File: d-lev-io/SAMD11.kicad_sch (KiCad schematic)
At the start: 32 parts, among them J6 PROG_HDR, SW1 SW_Push, SW2 SW_Push, SW3 SW_Push, U3 ATSAMD11D14A-M

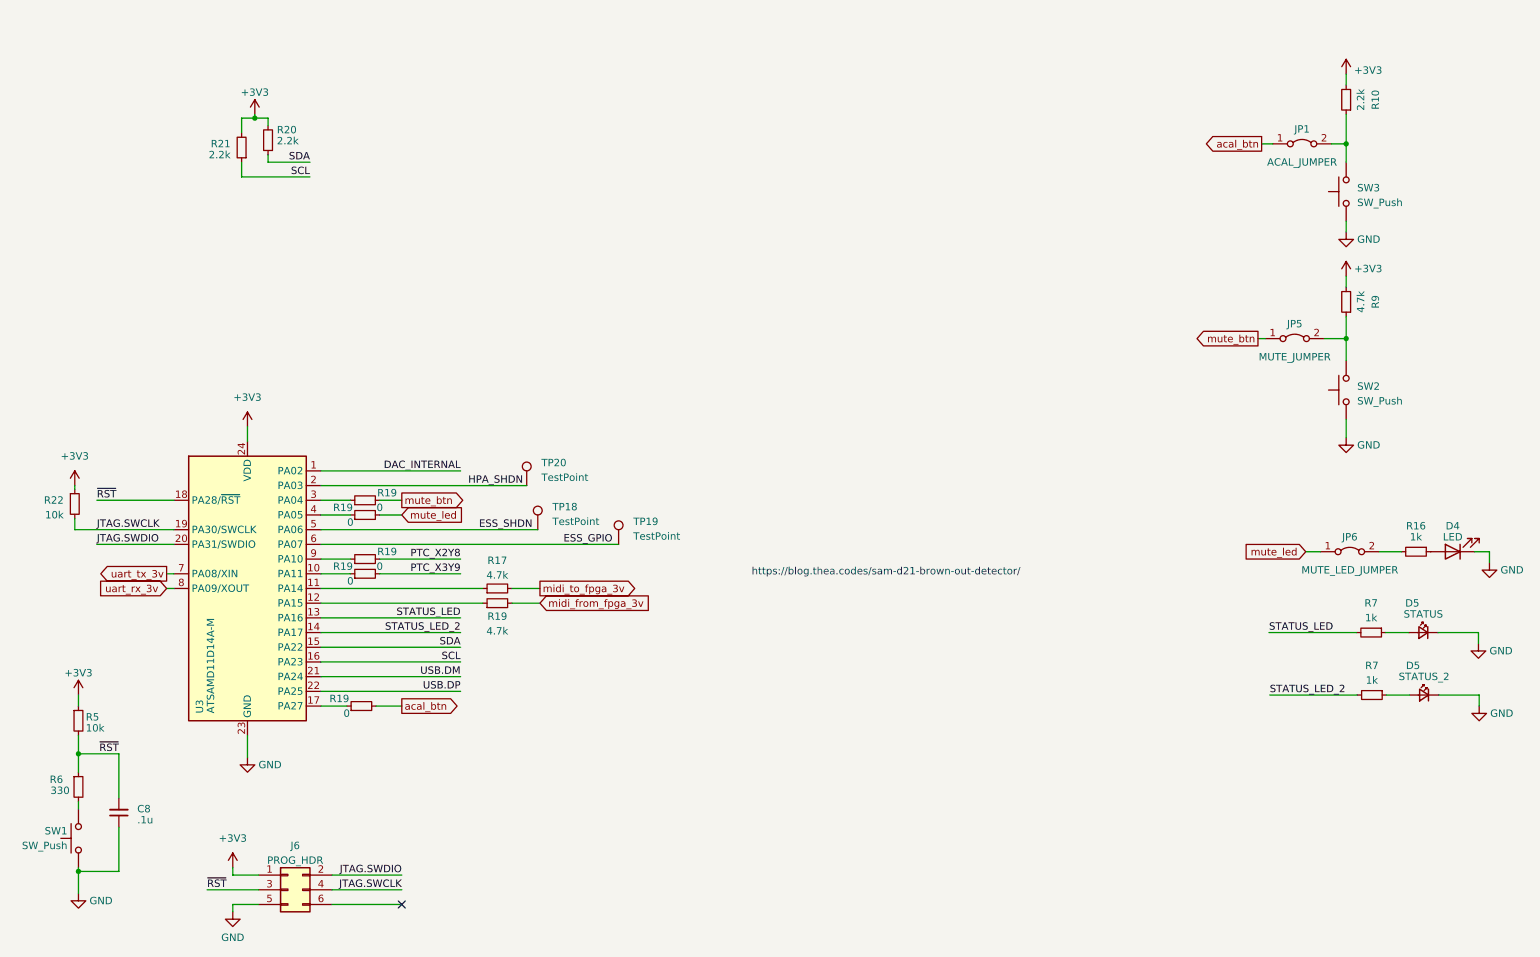
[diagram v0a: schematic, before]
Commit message: Added DAC schematic to I/O board
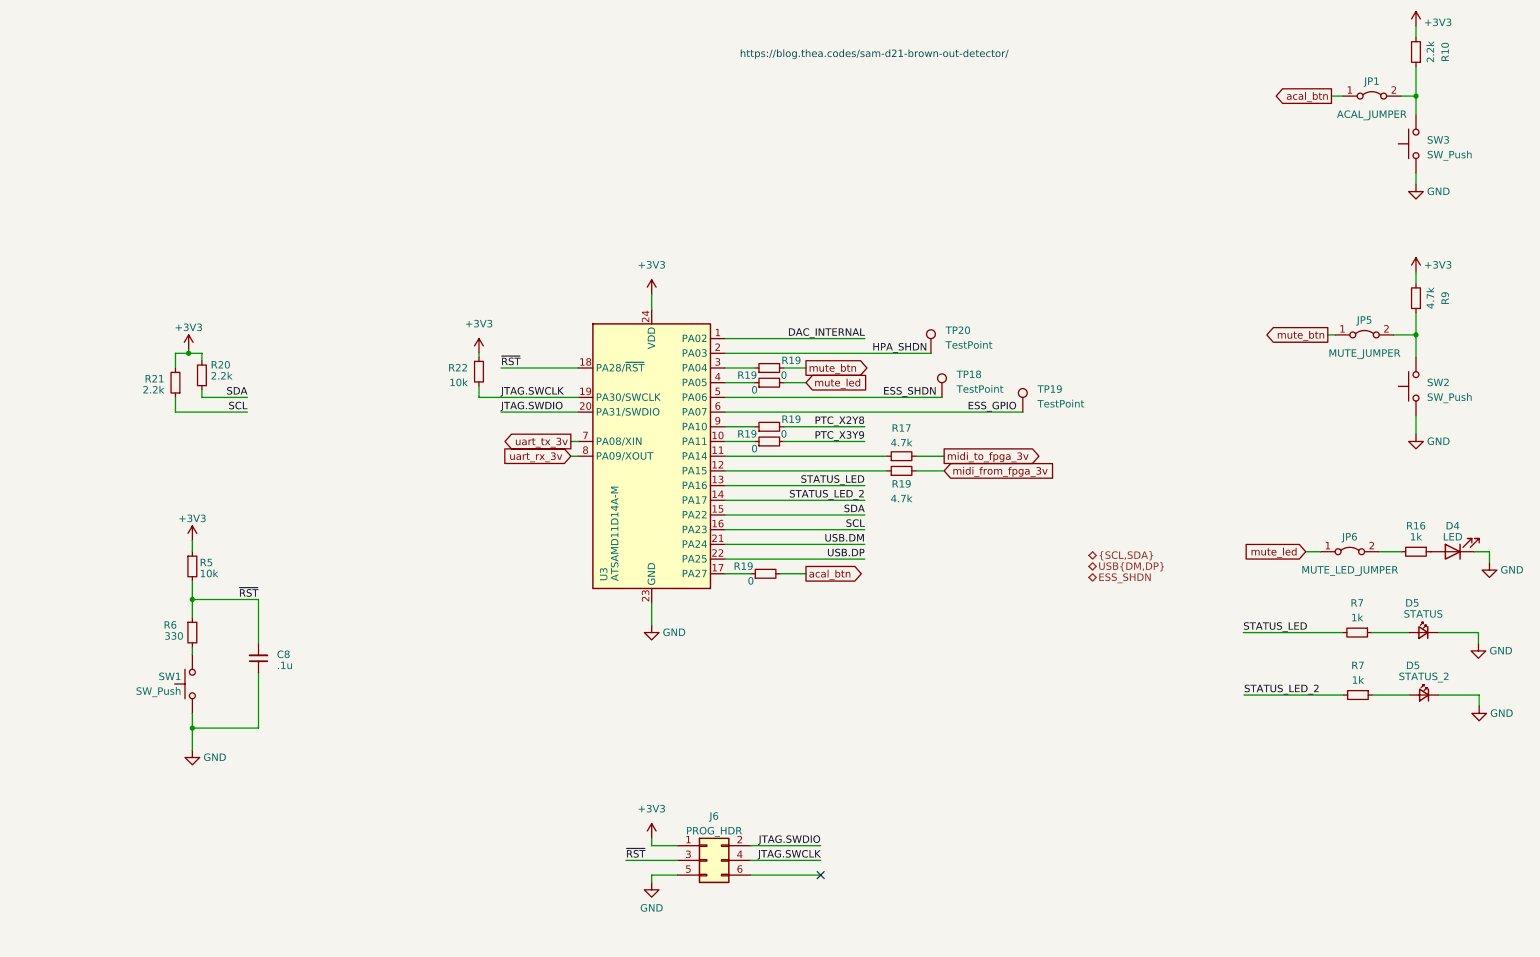
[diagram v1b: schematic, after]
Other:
- moved on the sheet: C8, J6, JP1, JP5, R10, R17, R19, R20, R21, R22, R5, R6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

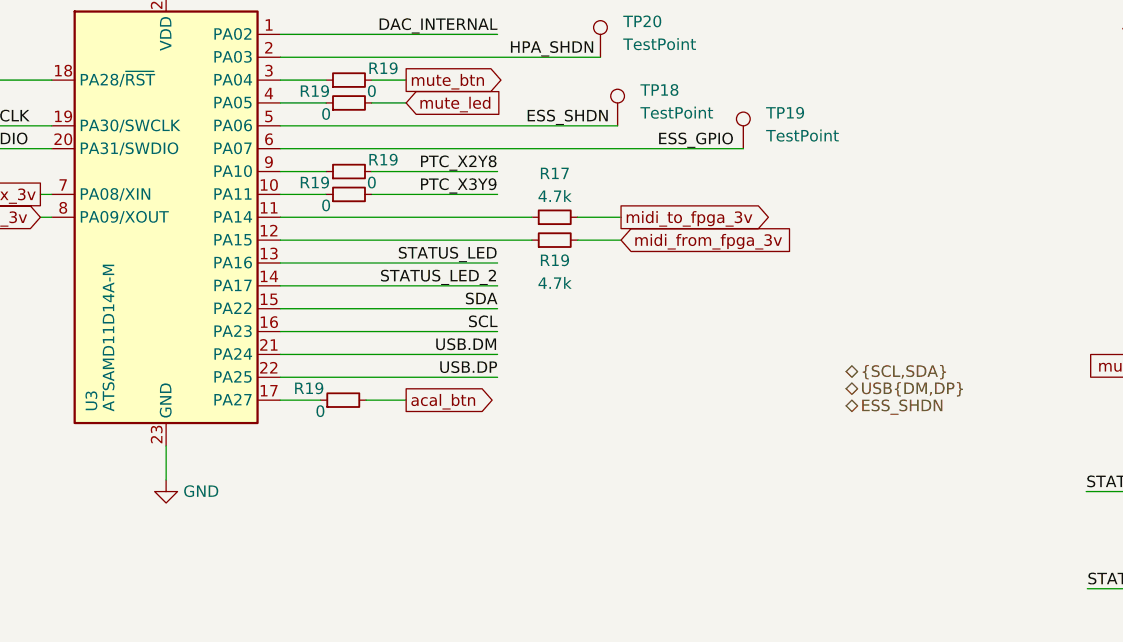
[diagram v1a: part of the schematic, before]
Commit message: add headphone amp
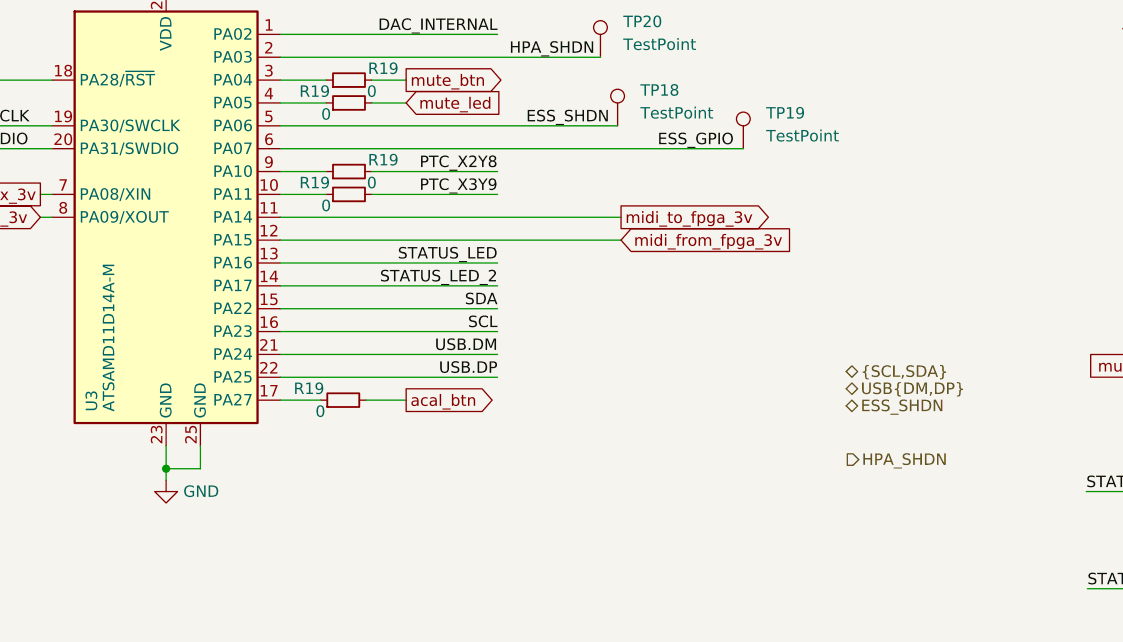
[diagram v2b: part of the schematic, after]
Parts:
- removed R17, R19: 4.7k, Resistor_SMD:R_0603_1608Metric, symbol Device:R_Small
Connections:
- net GND: now also U3.25 (GND)
- net midi_from_fpga_3v: now also U3.12 (PA15)
- net midi_to_fpga_3v: now also U3.11 (PA14)
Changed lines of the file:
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@@
   (junction (at 261.62 85.725) (diameter 0) (color 0 0 0 0)
+  )
+  (junction (at 129.54 134.62) (diameter 0) (color 0 0 0 0)
   )
   (junction (at 261.62 44.45) (diameter 0) (color 0 0 0 0)
@@
     (stroke (width 0) (type default))
   )
-  (wire (pts (xy 170.18 106.68) (xy 142.24 106.68))
-    (stroke (width 0) (type default))
-  )
   (wire (pts (xy 142.24 116.84) (xy 166.37 116.84))
     (stroke (width 0) (type default))
@@
     (stroke (width 0) (type default))
   )
+  (wire (pts (xy 129.54 134.62) (xy 129.54 132.08))
+    (stroke (width 0) (type default))
+  )
   (wire (pts (xy 142.24 96.52) (xy 179.705 96.52))
     (stroke (width 0) (type default))
   )
+  (wire (pts (xy 133.35 134.62) (xy 129.54 134.62))
+    (stroke (width 0) (type default))
+  )
   (wire (pts (xy 259.08 44.45) (xy 261.62 44.45))
     (stroke (width 0) (type default))
@@
     (stroke (width 0) (type default))
   )
-  (wire (pts (xy 175.26 109.22) (xy 180.086 109.22))
-    (stroke (width 0) (type default))
-  )
-  (wire (pts (xy 129.54 135.89) (xy 129.54 132.08))
+  (wire (pts (xy 129.54 135.89) (xy 129.54 134.62))
     (stroke (width 0) (type default))
   )
@@
     (stroke (width 0) (type default))
   )
+  (wire (pts (xy 133.35 132.08) (xy 133.35 134.62))
+    (stroke (width 0) (type default))
+  )
   (wire (pts (xy 261.62 81.915) (xy 261.62 85.725))
     (stroke (width 0) (type default))
@@
     (stroke (width 0) (type default))
   )
-  (wire (pts (xy 175.26 106.68) (xy 180.086 106.68))
-    (stroke (width 0) (type default))
-  )
   (wire (pts (xy 50.165 153.67) (xy 50.165 157.48))
     (stroke (width 0) (type default))
@@
     (stroke (width 0) (type default))
   )
+  (wire (pts (xy 142.24 106.68) (xy 180.086 106.68))
+    (stroke (width 0) (type default))
+  )
   (wire (pts (xy 156.21 93.98) (xy 152.4 93.98))
     (stroke (width 0) (type default))
@@
     (stroke (width 0) (type default))
   )
-  (wire (pts (xy 170.18 109.22) (xy 142.24 109.22))
+  (wire (pts (xy 142.24 109.22) (xy 180.086 109.22))
     (stroke (width 0) (type default))
   )
@@
     (effects (font (size 1.27 1.27)) (justify left))
   )
+  (hierarchical_label "HPA_SHDN" (shape output) (at 205.232 133.604 0) (fields_autoplaced)
+    (effects (font (size 1.27 1.27)) (justify left))
+  )
   (hierarchical_label "{SCL,SDA}" (shape bidirectional) (at 205.105 123.825 0) (fields_autoplaced)
     (effects (font (size 1.27 1.27)) (justify left))
@@
     )
   )
-  (symbol (lib_id "Device:R_Small") (at 172.72 109.22 90) (unit 1)
-    (in_bom yes) (on_board yes) (dnp no)
-    (property "Reference" "R19" (at 172.72 111.506 90)
-      (effects (font (size 1.27 1.27)))
-    )
-    (property "Value" "4.7k" (at 172.72 114.046 90)
-      (effects (font (size 1.27 1.27)))
-    )
-    (property "Footprint" "Resistor_SMD:R_0603_1608Metric" (at 172.72 109.22 0)
-      (effects (font (size 1.27 1.27)) hide)
-    )
-    (property "Datasheet" "~" (at 172.72 109.22 0)
-      (effects (font (size 1.27 1.27)) hide)
-    )
-    (pin "1")
-    (pin "2")
-    (instances
-      (project "d-lev-io"
-        (path "/9261a07b-ae4a-4d72-8042-ea097cd0e5ed"
-          (reference "R19") (unit 1)
-        )
-        (path "/9261a07b-ae4a-4d72-8042-ea097cd0e5ed/fd6a6c10-f456-4937-8c5d-f097bbb805c0"
-          (reference "R19") (unit 1)
-        )
-      )
-    )
-  )
   (symbol (lib_id "power:GND") (at 129.54 135.89 0) (unit 1)
     (in_bom yes) (on_board yes) (dnp no) (fields_autoplaced)
@@
     )
   )
-  (symbol (lib_id "Device:R_Small") (at 172.72 106.68 90) (unit 1)
-    (in_bom yes) (on_board yes) (dnp no)
-    (property "Reference" "R17" (at 172.72 101.854 90)
-      (effects (font (size 1.27 1.27)))
-    )
-    (property "Value" "4.7k" (at 172.72 104.394 90)
-      (effects (font (size 1.27 1.27)))
-    )
-    (property "Footprint" "Resistor_SMD:R_0603_1608Metric" (at 172.72 106.68 0)
-      (effects (font (size 1.27 1.27)) hide)
-    )
-    (property "Datasheet" "~" (at 172.72 106.68 0)
-      (effects (font (size 1.27 1.27)) hide)
-    )
-    (pin "1")
-    (pin "2")
-    (instances
-      (project "d-lev-io"
-        (path "/9261a07b-ae4a-4d72-8042-ea097cd0e5ed"
-          (reference "R17") (unit 1)
-        )
-        (path "/9261a07b-ae4a-4d72-8042-ea097cd0e5ed/fd6a6c10-f456-4937-8c5d-f097bbb805c0"
-          (reference "R17") (unit 1)
-        )
-      )
-    )
-  )
   (symbol (lib_id "Device:R_Small") (at 149.86 101.6 90) (unit 1)
     (in_bom yes) (on_board yes) (dnp no)
@@
       (effects (font (size 1.27 1.27)) hide)
     )
+    (pin "25")
     (pin "1")
     (pin "10")
